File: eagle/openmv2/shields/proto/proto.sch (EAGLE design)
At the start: 2 parts

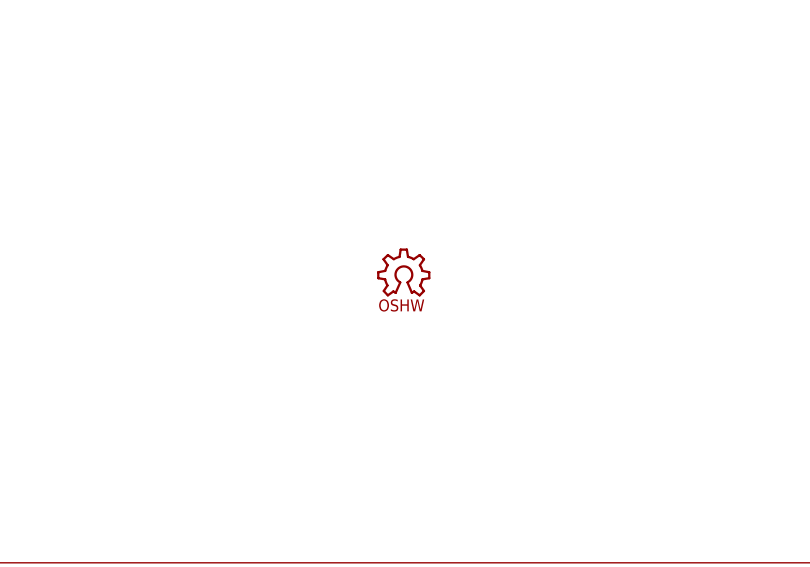
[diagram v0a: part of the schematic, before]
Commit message: Update shields silk-screen.
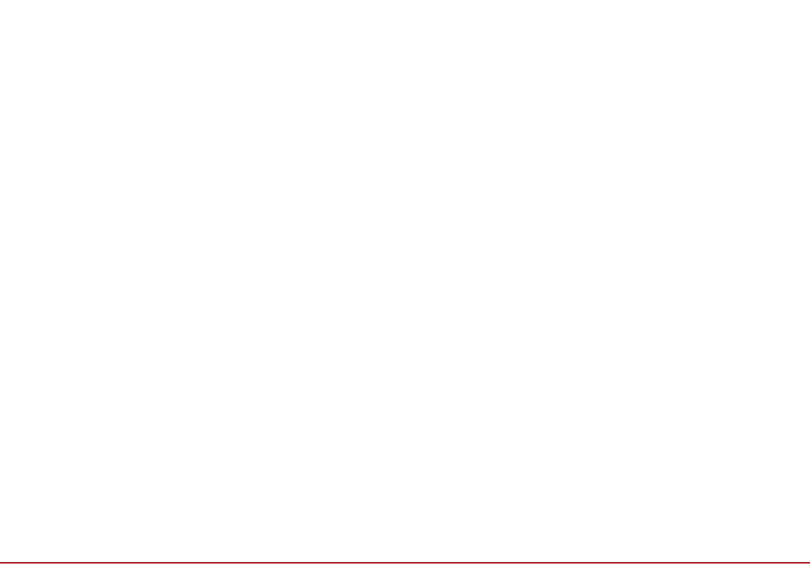
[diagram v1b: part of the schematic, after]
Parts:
- removed LOGO1: OSHW_LOGO_8MILX0150-NT, iofault:OSHW_LOGO_8MILX0150-NT
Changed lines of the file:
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@@
 <part name="U$2" library="openmv" deviceset="OPENMV3" device=""/>
 <part name="P+4" library="sfe" deviceset="3.3V" device=""/>
-<part name="LOGO1" library="iofault" deviceset="OSHW_LOGO_8MIL" device="X0150-NT"/>
 </parts>
 <sheets>
@@
 <instance part="U$2" gate="G$1" x="132.08" y="73.66"/>
 <instance part="P+4" gate="G$1" x="104.14" y="93.98"/>
-<instance part="LOGO1" gate="G$1" x="205.74" y="27.94"/>
 </instances>
 <busses>
